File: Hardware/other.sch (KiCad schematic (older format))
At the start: 33 parts, among them J10 TILT, J12 POWER ON, J5 Debug, J7 I2C INTERNAL, J8 B5B-XH-A__LF__SN_, J9 B8B-XH-A_LF__SN_, Q6 IRLML6244TRPBF, Q7 FDC638P

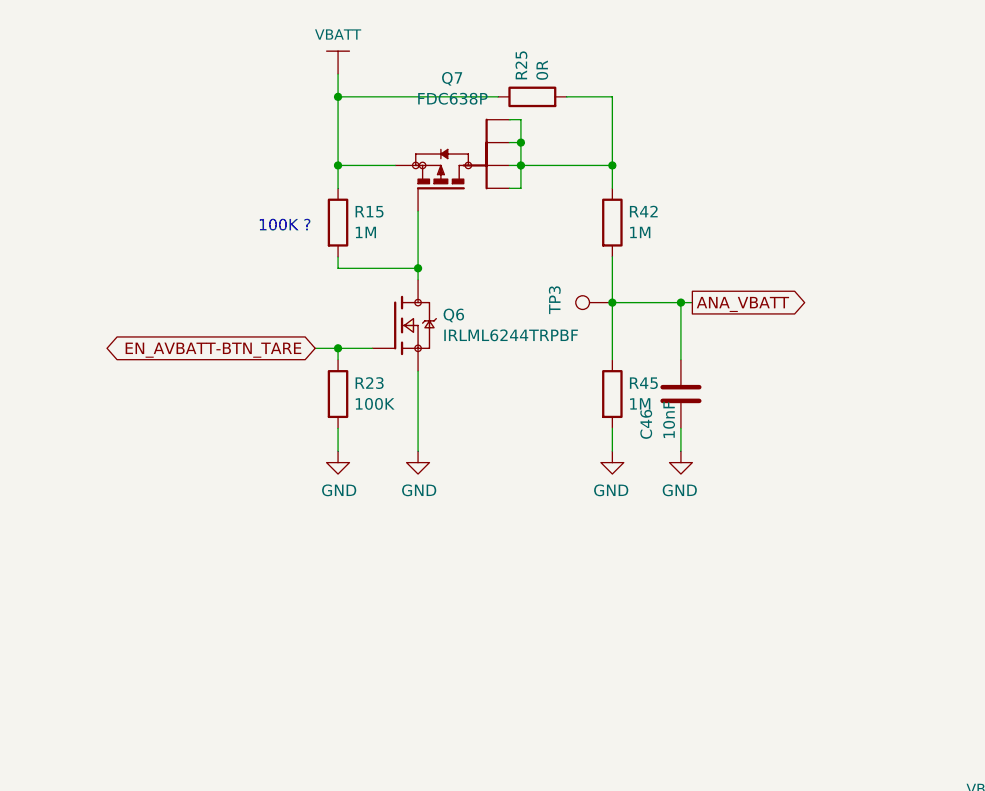
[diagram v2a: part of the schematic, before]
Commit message: Add Gerber files, Bom, Jlcpcb LCSC parts ref, some optimizations
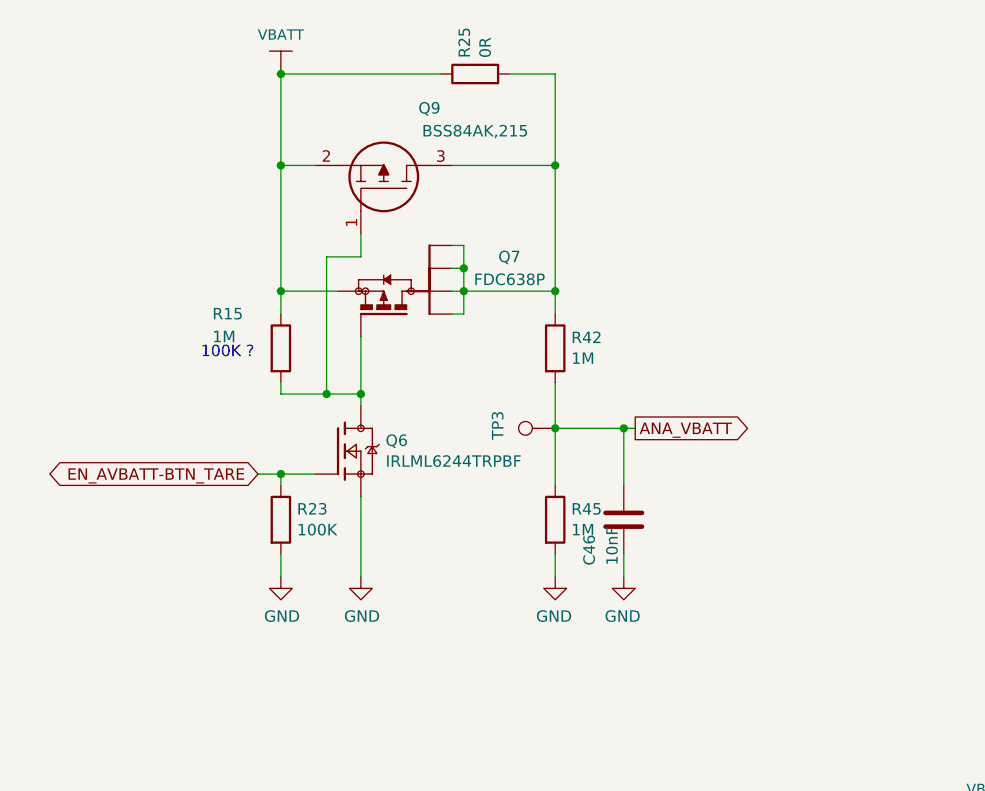
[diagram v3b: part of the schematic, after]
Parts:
- added Q9: BSS84AK,215, EcoApi_pcb:SOT95P230X110-3N, symbol EcoApi_pcb:BSS84AK,215
- C30, C31, C32: Dielectric (none) -> X7R; JLC (none) -> 0603; LCSC (none) -> C1591; Manufacturer_Name (none) -> Samsung Electro-Mechanics; Manufacturer_Part_Number (none) -> CL10B104KB8NNNC; Tolerance (none) -> 10%; Voltage (none) -> 50V
- C46: Dielectric (none) -> X7R; JLC (none) -> 0603; LCSC (none) -> C100042; Manufacturer_Name (none) -> Samsung Electro-Mechanics; Manufacturer_Part_Number (none) -> CL10B103KB8NNNC; Tolerance (none) -> 10%; Voltage (none) -> 50V
- D7: Populate yes -> no
- Q6: JLC (none) -> SOT-23-3; LCSC (none) -> C143946
- Q7: JLC (none) -> SSOT-6; Populate yes -> no
- R15, R42, R45, R65: JLC (none) -> 0603; LCSC (none) -> C22935; Manufacturer_Name (none) -> UNI-ROYAL(Uniroyal Elec); Manufacturer_Part_Number (none) -> 0603WAF1004T5E; Power Rating (none) -> 1/10W; Voltage (none) -> 75V
- R23: JLC (none) -> 0603; LCSC (none) -> C25803; Manufacturer_Name (none) -> UNI-ROYAL(Uniroyal Elec); Manufacturer_Part_Number (none) -> 0603WAF1003T5E; Power Rating (none) -> 1/10W; Voltage (none) -> 75V
- R25, R63: JLC (none) -> 0603; LCSC (none) -> C21189; Manufacturer_Name (none) -> UNI-ROYAL(Uniroyal Elec); Manufacturer_Part_Number (none) -> 0603WAF0000T5E; Power Rating (none) -> 1/10W; Voltage (none) -> 75V
- R46, R56: JLC (none) -> 1206; LCSC (none) -> C17888; Manufacturer_Name (none) -> UNI-ROYAL(Uniroyal Elec); Manufacturer_Part_Number (none) -> 1206W4F0000T5E; Power Rating (none) -> 1/4W; Voltage (none) -> 200V
- R67, R68, R69, R71, R73: JLC (none) -> 0603; LCSC (none) -> C25804; Manufacturer_Name (none) -> UNI-ROYAL(Uniroyal Elec); Manufacturer_Part_Number (none) -> 0603WAF1002T5E; Power Rating (none) -> 1/10W; Voltage (none) -> 75V
- R72: JLC (none) -> 0603; LCSC (none) -> C22843; Manufacturer_Name (none) -> UNI-ROYAL(Uniroyal Elec); Manufacturer_Part_Number (none) -> 0603WAF1501T5E; Power Rating (none) -> 1/10W; Voltage (none) -> 75V
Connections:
- net VBATT: now also Q9.2
- net at Q7.1, Q7.2, Q7.5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: now also Q9.3
- net at Q6.3, Q7.3, R15.2: now also Q9.1
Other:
- moved on the sheet: C46, Q6, Q7, R15, R23, R25, R42, R45, TP3

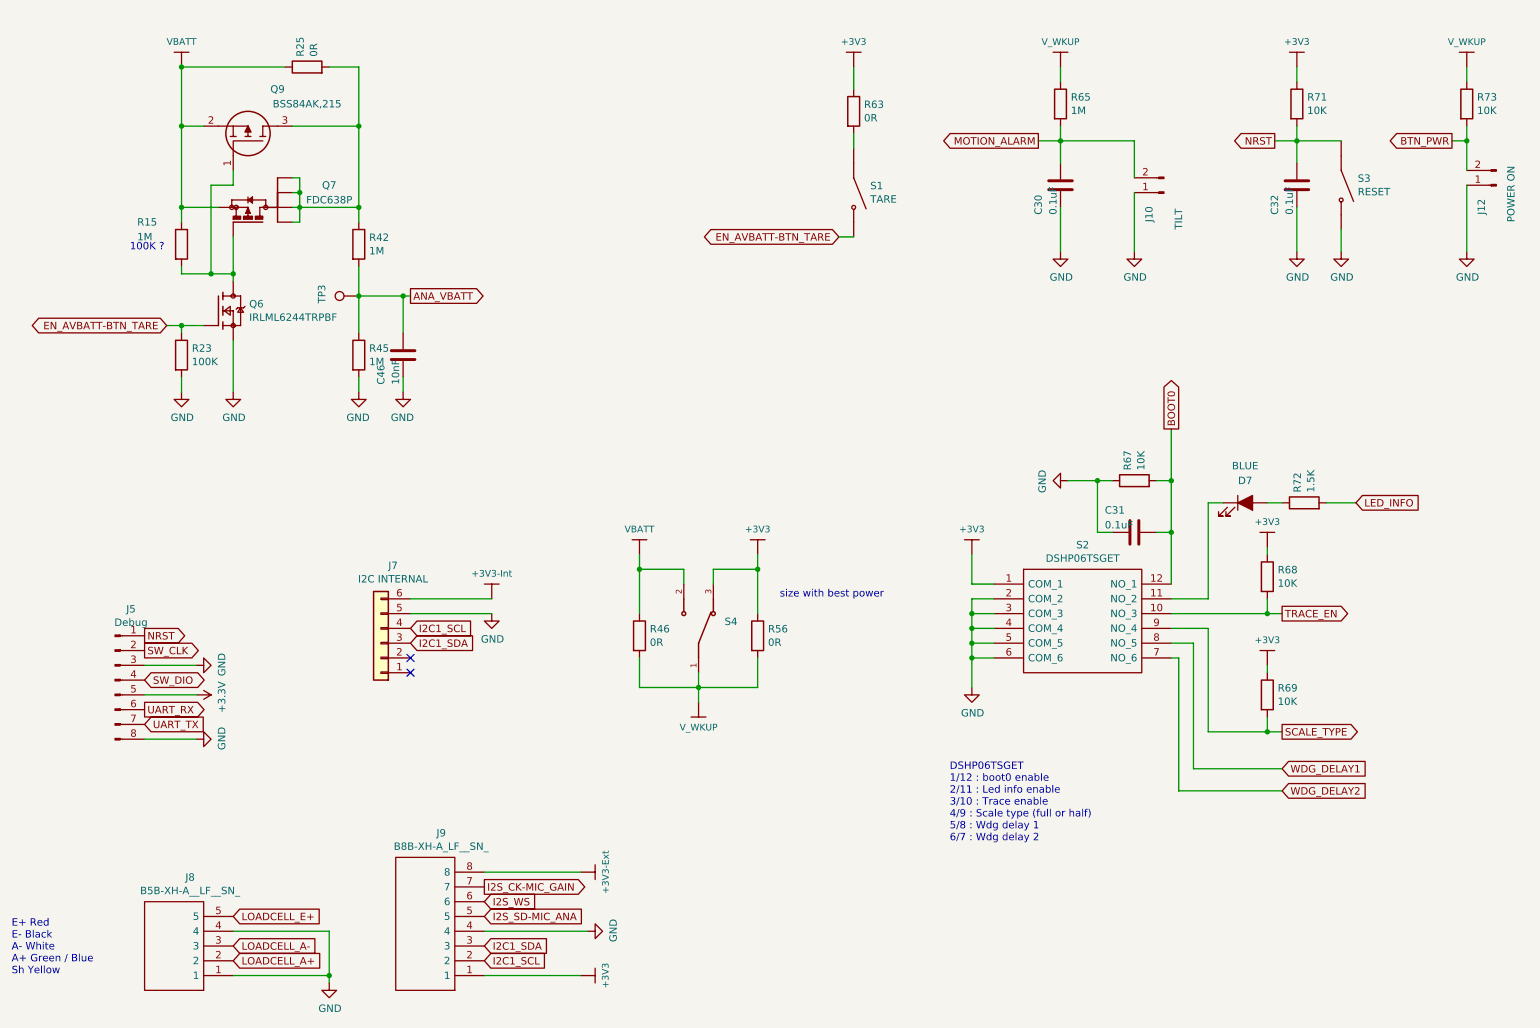
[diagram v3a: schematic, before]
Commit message: Fix JLCPCB assembly issues, Add reverse battery protection, Define Correct crystal capa, Add Layer number and fiducial, and some quicq fix
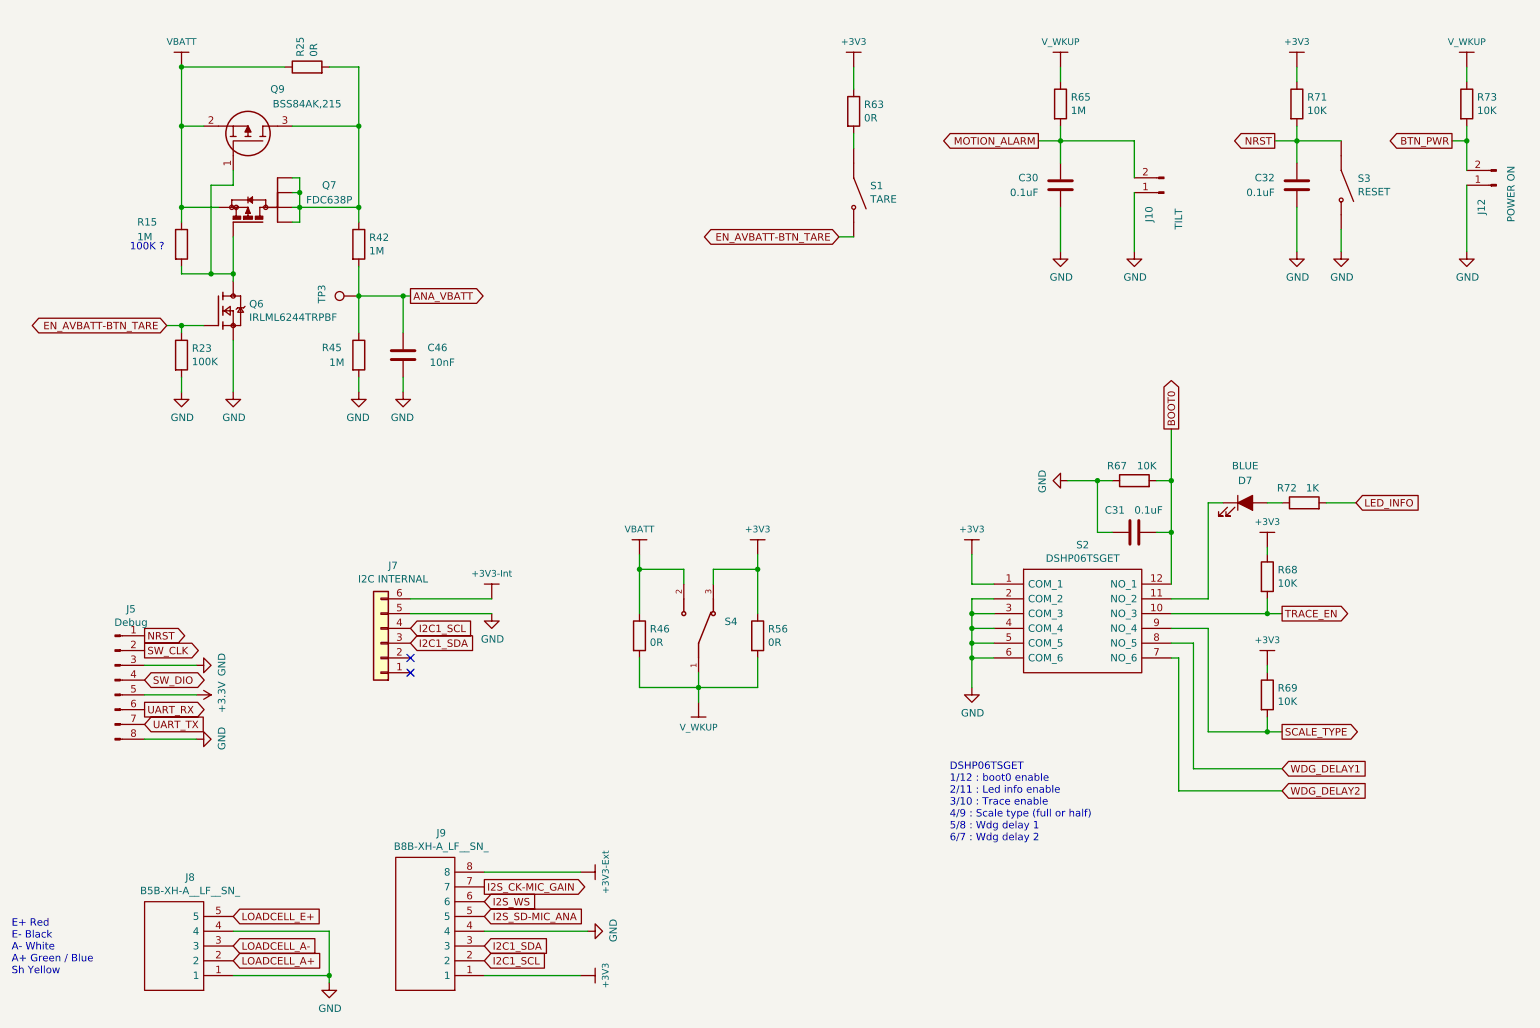
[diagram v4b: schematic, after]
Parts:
- R25: LCSC C21189 -> NM_C21189
- R46, R56: LCSC C17888 -> NM_C17888
- R72: value 1.5K -> 1K; LCSC C22843 -> C21190; Manufacturer_Part_Number 0603WAF1501T5E -> 0603WAF1001T5E
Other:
- note removed: "size with best power"
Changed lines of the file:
@@
 AR Path="/62CC297B/61E97F4A" Ref="C?"  Part="1"
 AR Path="/61B961C0/61E97F4A" Ref="C30"  Part="1"
-F 0 "C30" V 8050 1600 50  0000 L CNN
-F 1 "0.1uF" V 7950 1600 50  0000 L CNN
+F 0 "C30" H 8050 1850 50  0000 L CNN
+F 1 "0.1uF" H 8050 1750 50  0000 L CNN
 F 2 "Capacitor_SMD:C_0603_1608Metric" H 7938 1650 50  0001 C CNN
 F 3 "~" H 7900 1800 50  0001 C CNN
@@
 AR Path="/62CC297B/61ED30F2" Ref="R?"  Part="1"
 AR Path="/61B961C0/61ED30F2" Ref="R72"  Part="1"
-F 0 "R72" H 9620 3996 50  0000 L CNN
-F 1 "1.5K" H 9620 3905 50  0000 L CNN
+F 0 "R72" V 9650 4000 50  0000 L CNN
+F 1 "1K" V 9650 3850 50  0000 L CNN
 F 2 "Resistor_SMD:R_0603_1608Metric" V 9480 3950 50  0001 C CNN
 F 3 "~" H 9550 3950 50  0001 C CNN
@@
 F 7 "1%" H 9550 3950 50  0001 C CNN "Tolerance"
 F 8 "0603" H 9550 3950 50  0001 C CNN "JLC"
-F 9 "C22843" H 9550 3950 50  0001 C CNN "LCSC"
+F 9 "C21190" H 9550 3950 50  0001 C CNN "LCSC"
 F 10 "UNI-ROYAL(Uniroyal Elec)" H 9550 3950 50  0001 C CNN "Manufacturer_Name"
-F 11 "0603WAF1501T5E" H 9550 3950 50  0001 C CNN "Manufacturer_Part_Number"
+F 11 "0603WAF1001T5E" H 9550 3950 50  0001 C CNN "Manufacturer_Part_Number"
 F 12 "1/10W" H 9550 3950 50  0001 C CNN "Power Rating"
 F 13 "75V" H 9550 3950 50  0001 C CNN "Voltage"
@@
 AR Path="/61B961C0/621F0FF4" Ref="C31"  Part="1"
 F 0 "C31" V 8550 3950 50  0000 L CNN
-F 1 "0.1uF" V 8450 3950 50  0000 L CNN
+F 1 "0.1uF" V 8550 4150 50  0000 L CNN
 F 2 "Capacitor_SMD:C_0603_1608Metric" H 8438 4000 50  0001 C CNN
 F 3 "~" H 8400 4150 50  0001 C CNN
@@
 AR Path="/62B8145A/621DB7B2" Ref="R?"  Part="1"
 AR Path="/61B961C0/621DB7B2" Ref="R67"  Part="1"
-F 0 "R67" H 8470 3846 50  0000 L CNN
-F 1 "10K" H 8470 3755 50  0000 L CNN
+F 0 "R67" V 8500 3850 50  0000 L CNN
+F 1 "10K" V 8500 3650 50  0000 L CNN
 F 2 "Resistor_SMD:R_0603_1608Metric" V 8330 3800 50  0001 C CNN
 F 3 "~" H 8400 3800 50  0001 C CNN
@@
 AR Path="/62CC297B/629B6680" Ref="C?"  Part="1"
 AR Path="/61B961C0/629B6680" Ref="C32"  Part="1"
-F 0 "C32" V 9650 1600 50  0000 L CNN
-F 1 "0.1uF" V 9550 1600 50  0000 L CNN
+F 0 "C32" H 9650 1850 50  0000 L CNN
+F 1 "0.1uF" H 9650 1750 50  0000 L CNN
 F 2 "Capacitor_SMD:C_0603_1608Metric" H 9538 1650 50  0001 C CNN
 F 3 "~" H 9500 1800 50  0001 C CNN
@@
 F 7 "1%" H 5050 4850 50  0001 C CNN "Tolerance"
 F 8 "1206" H 5050 4850 50  0001 C CNN "JLC"
-F 9 "C17888" H 5050 4850 50  0001 C CNN "LCSC"
+F 9 "NM_C17888" H 5050 4850 50  0001 C CNN "LCSC"
 F 10 "UNI-ROYAL(Uniroyal Elec)" H 5050 4850 50  0001 C CNN "Manufacturer_Name"
 F 11 "1206W4F0000T5E" H 5050 4850 50  0001 C CNN "Manufacturer_Part_Number"
@@
 F 7 "1%" H 5850 4850 50  0001 C CNN "Tolerance"
 F 8 "1206" H 5850 4850 50  0001 C CNN "JLC"
-F 9 "C17888" H 5850 4850 50  0001 C CNN "LCSC"
+F 9 "NM_C17888" H 5850 4850 50  0001 C CNN "LCSC"
 F 10 "UNI-ROYAL(Uniroyal Elec)" H 5850 4850 50  0001 C CNN "Manufacturer_Name"
 F 11 "1206W4F0000T5E" H 5850 4850 50  0001 C CNN "Manufacturer_Part_Number"
@@
 Wire Wire Line
 	5050 5200 5450 5200
-Text Notes 6000 4600 0    50   ~ 0
-size with best power
 Text GLabel 3500 2550 2    50   Output ~ 0
 ANA_VBATT
@@
 AR Path="/62CC297B/62762A44" Ref="R?"  Part="1"
 AR Path="/61B961C0/62762A44" Ref="R45"  Part="1"
-F 0 "R45" H 3220 2996 50  0000 L CNN
-F 1 "1M" H 3220 2905 50  0000 L CNN
+F 0 "R45" H 2900 3000 50  0000 L CNN
+F 1 "1M" H 2950 2900 50  0000 L CNN
 F 2 "Resistor_SMD:R_0603_1608Metric" V 3080 2950 50  0001 C CNN
 F 3 "~" H 3150 2950 50  0001 C CNN
@@
 AR Path="/62CC297B/62762A57" Ref="C?"  Part="1"
 AR Path="/61B961C0/62762A57" Ref="C46"  Part="1"
-F 0 "C46" V 3600 2750 50  0000 L CNN
-F 1 "10nF" V 3500 2750 50  0000 L CNN
+F 0 "C46" H 3150 3000 50  0000 L CNN
+F 1 "10nF" H 3100 2900 50  0000 L CNN
 F 2 "Capacitor_SMD:C_0603_1608Metric" H 3488 2800 50  0001 C CNN
 F 3 "~" H 3450 2950 50  0001 C CNN
@@
 F 7 "1%" H 2800 1000 50  0001 C CNN "Tolerance"
 F 8 "0603" H 2800 1000 50  0001 C CNN "JLC"
-F 9 "C21189" H 2800 1000 50  0001 C CNN "LCSC"
+F 9 "NM_C21189" H 2800 1000 50  0001 C CNN "LCSC"
 F 10 "UNI-ROYAL(Uniroyal Elec)" H 2800 1000 50  0001 C CNN "Manufacturer_Name"
 F 11 "0603WAF0000T5E" H 2800 1000 50  0001 C CNN "Manufacturer_Part_Number"

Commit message: Debug some features on hardware
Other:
- note added: "C46 = 100nF"
- note added: "R45 = 2M"
- note added: "attention conflit avec 3v3 pullup i2c et 3v3-int !!!"
- note added: "enlever switch et VBAT == VWKUP"
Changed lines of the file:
@@
 Wire Wire Line
 	2150 2400 2300 2400
+Text Notes 2550 4300 0    50   ~ 0
+attention conflit avec 3v3 pullup i2c et 3v3-int !!!
+Text Notes 5150 4000 0    50   ~ 0
+enlever switch et VBAT == VWKUP
+Text Notes 2700 3200 0    50   ~ 0
+R45 = 2M
+Text Notes 3600 3150 0    50   ~ 0
+C46 = 100nF
 $EndSCHEMATC

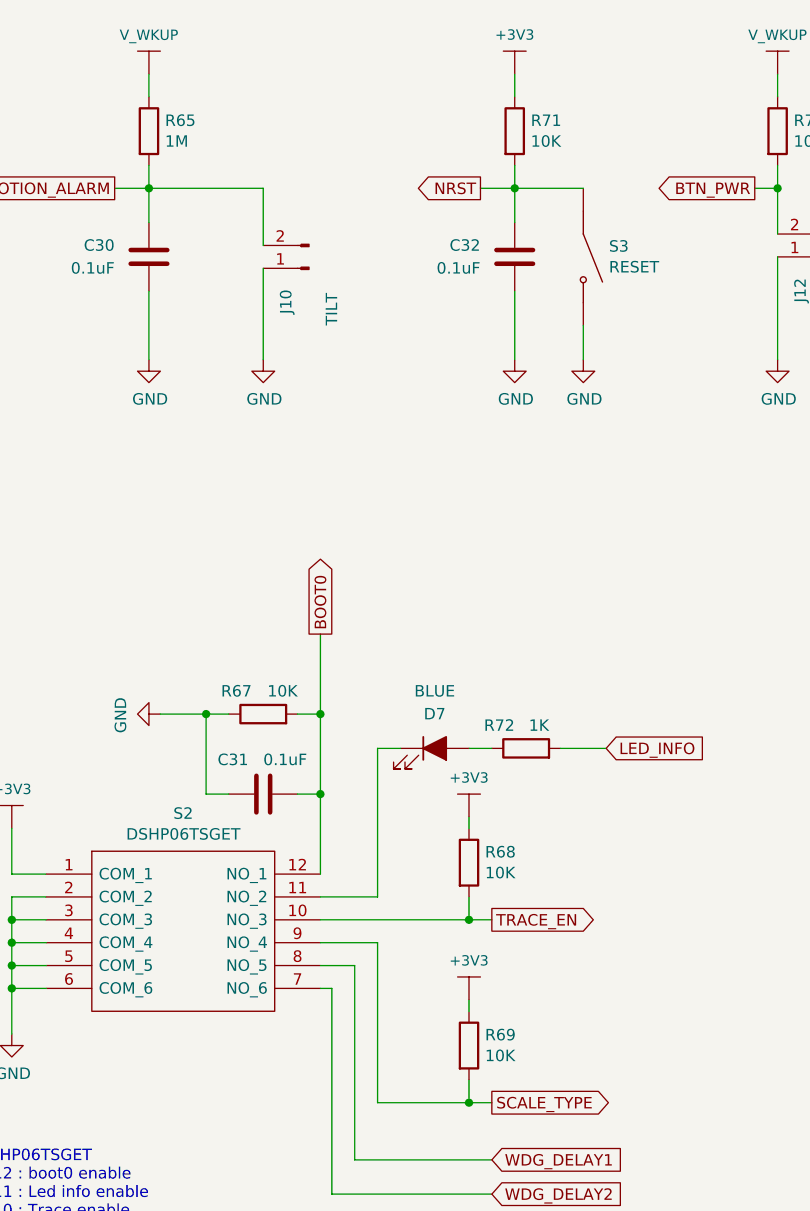
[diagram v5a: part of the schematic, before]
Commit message: Fix rtc write time, fix hx711 rate, Add offset for vbatt, start i2s dma mic
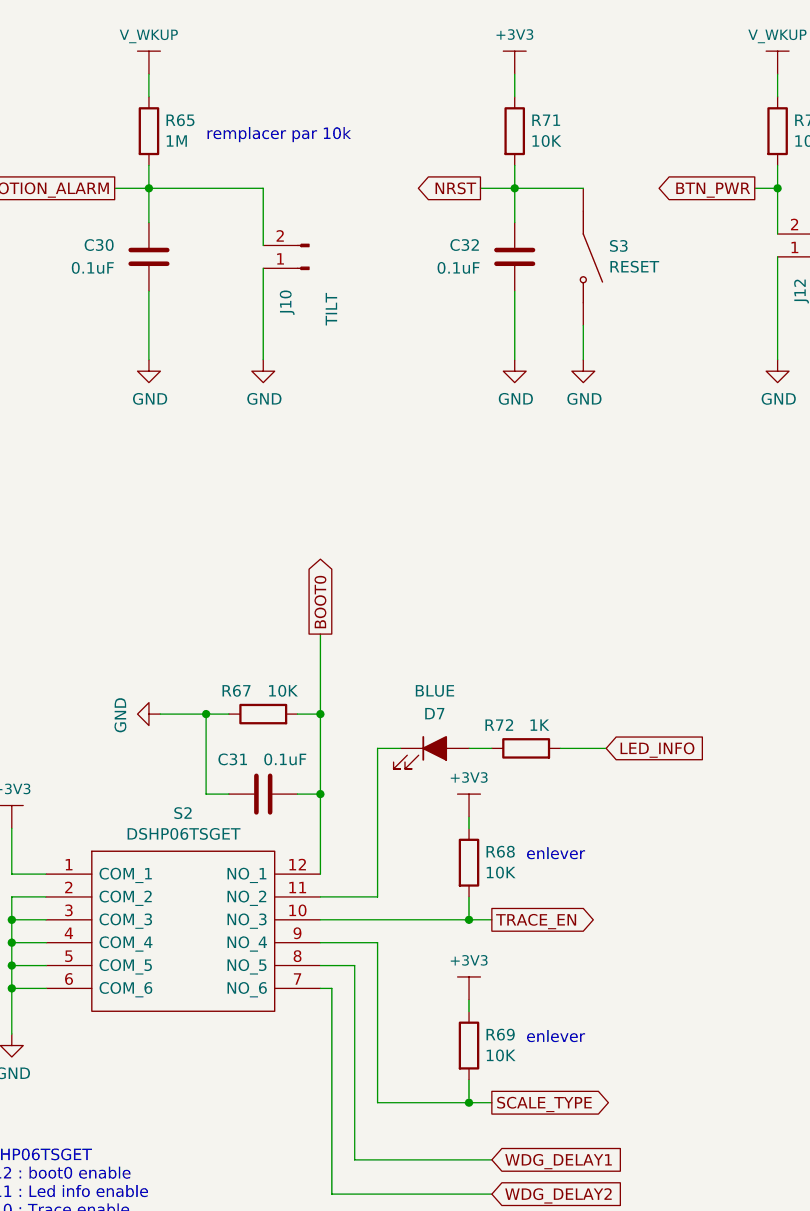
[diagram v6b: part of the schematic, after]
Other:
- note added: "enlever"
- note added: "remplacer par 10k"
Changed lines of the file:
@@
 Text Notes 3600 3150 0    50   ~ 0
 C46 = 100nF
+Text Notes 9550 4450 0    50   ~ 0
+enlever
+Text Notes 9550 5250 0    50   ~ 0
+enlever
+Text Notes 8150 1300 0    50   ~ 0
+remplacer par 10k
 $EndSCHEMATC
